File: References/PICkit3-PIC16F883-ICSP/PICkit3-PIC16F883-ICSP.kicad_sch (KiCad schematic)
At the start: 0 parts

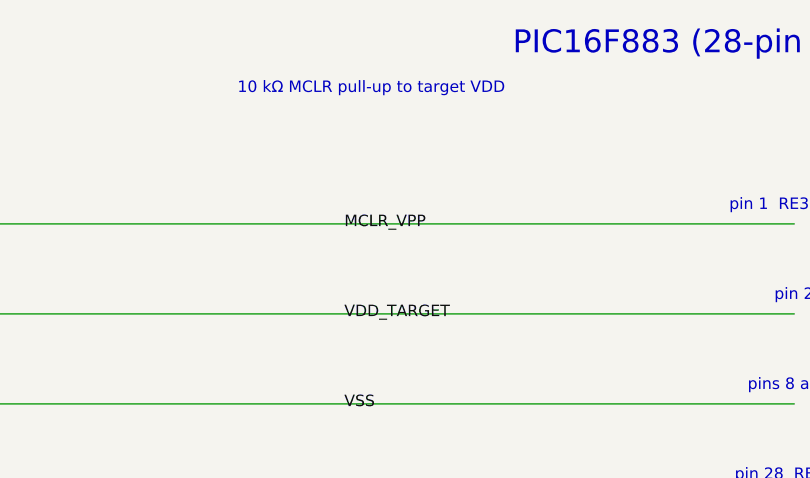
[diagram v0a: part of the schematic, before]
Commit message: Draw the MCLR pull-up as an actual resistor
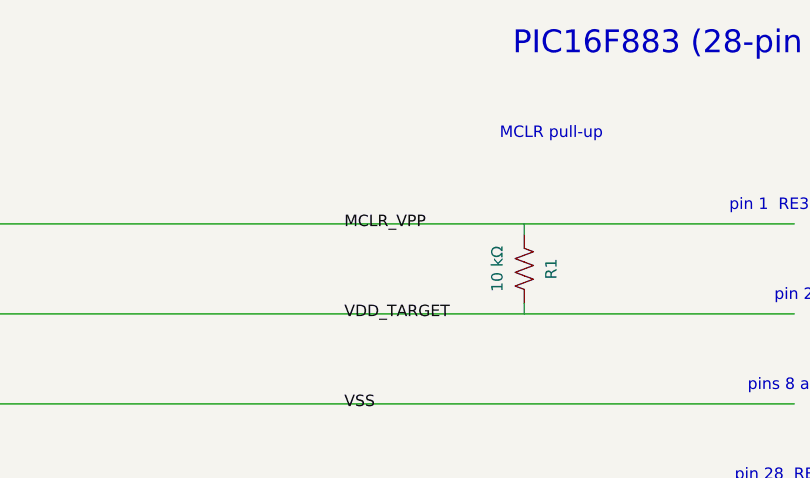
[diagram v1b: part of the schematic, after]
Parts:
- added R1: 10 kΩ, symbol Device:R_US
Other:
- note added: "MCLR pull-up"
- note removed: "10 kΩ MCLR pull-up to target VDD"
